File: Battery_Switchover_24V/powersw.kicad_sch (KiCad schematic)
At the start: 22 parts, among them U10 FDBL86066-F085, U2 LM74610QDGKRQ1, U5 LM74610QDGKRQ1

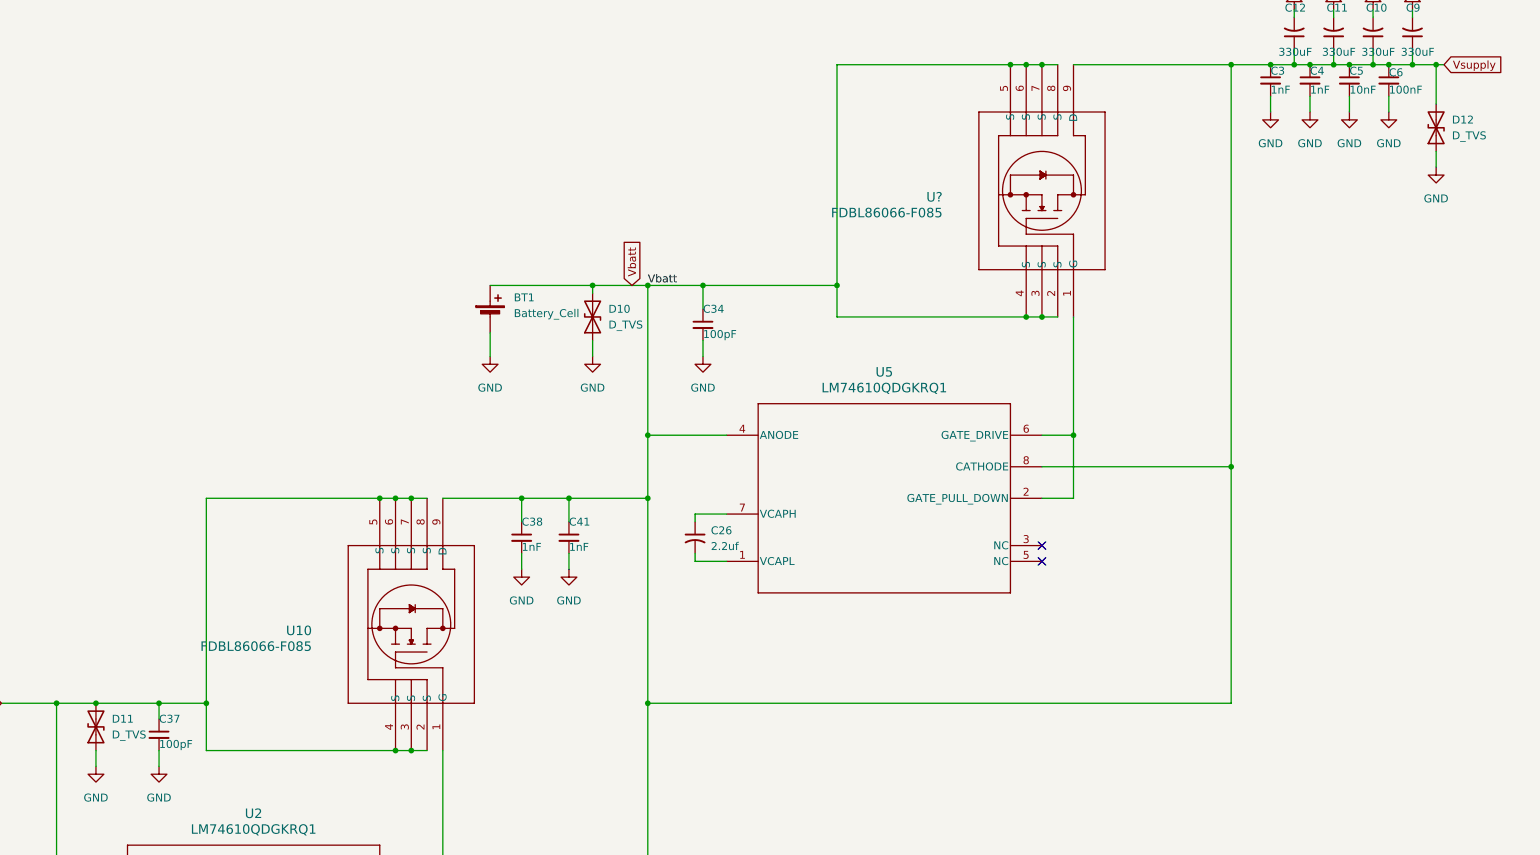
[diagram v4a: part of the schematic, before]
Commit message: Added some Model Numbers For TVS diodes
Added TVS diode model for ADC and
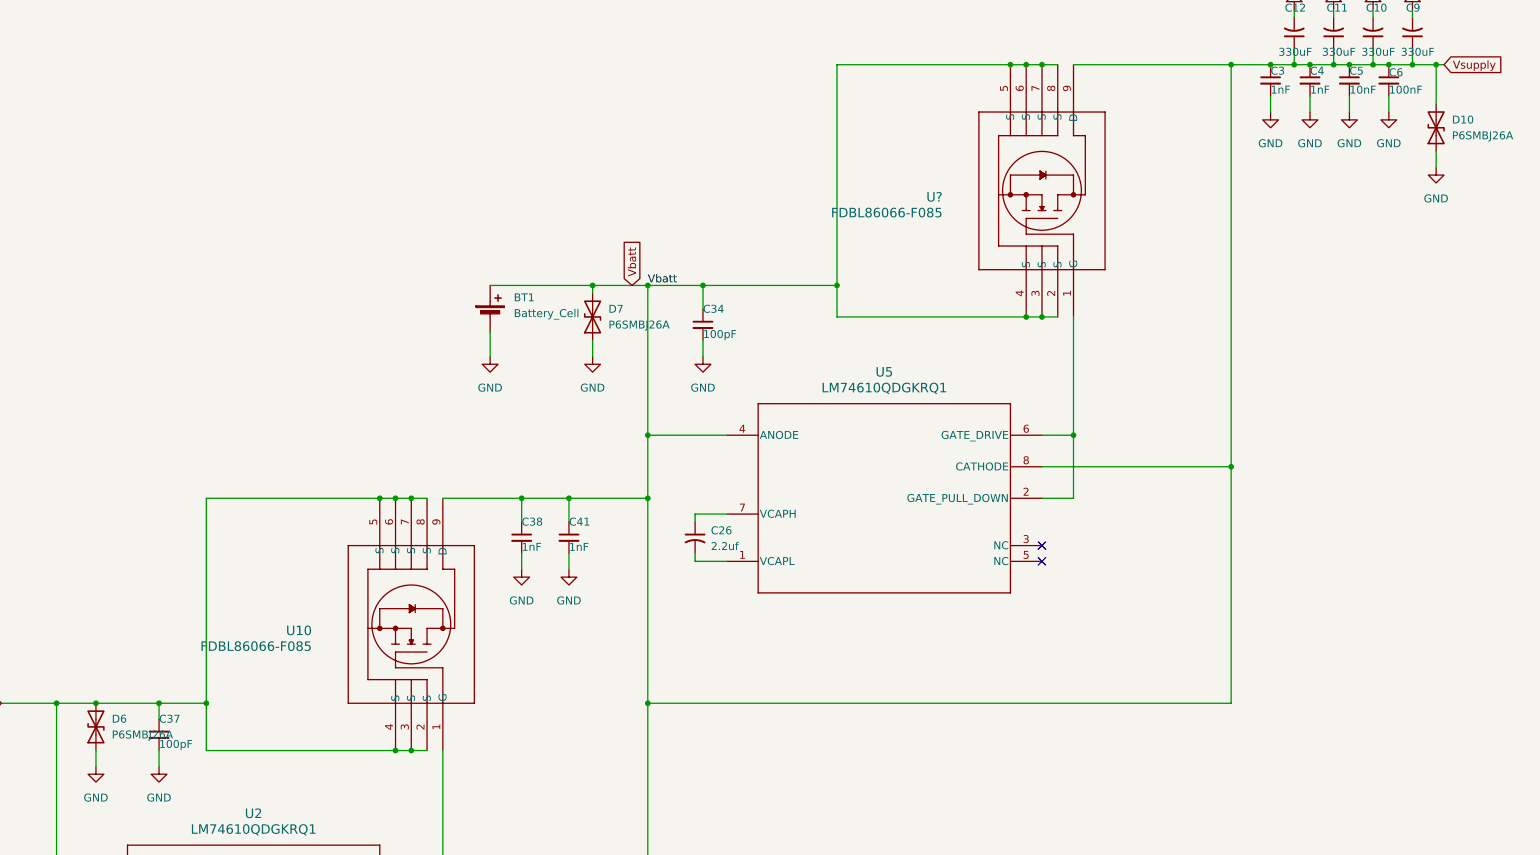
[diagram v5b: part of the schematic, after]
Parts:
- removed D11, D12: D_TVS, symbol Device:D_TVS
- added D6, D7: P6SMBJ26A, symbol Device:D_TVS
- D10: value D_TVS -> P6SMBJ26A
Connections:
- net GND: now also D6.1 (A1), D7.1 (A1)
- net Vbatt: now also D7.2 (A2)
- net Vin: now also D6.2 (A2)
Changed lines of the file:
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@@
 	)
 	(junction
+		(at 39.37 137.16)
+		(diameter 0)
+		(color 0 0 0 0)
+	)
+	(junction
 		(at 128.27 137.16)
 		(diameter 0)
@@
 	)
 	(junction
-		(at 39.37 137.16)
-		(diameter 0)
-		(color 0 0 0 0)
-	)
-	(junction
 		(at 119.38 69.85)
 		(diameter 0)
@@
 	(wire
 		(pts
+			(xy 39.37 137.16) (xy 49.53 137.16)
+		)
+		(stroke
+			(width 0)
+			(type default)
+		)
+	)
+	(wire
+		(pts
 			(xy 85.09 104.14) (xy 57.15 104.14)
 		)
@@
 	(wire
 		(pts
-			(xy 33.02 137.16) (xy 39.37 137.16)
-		)
-		(stroke
-			(width 0)
-			(type default)
-		)
-	)
-	(wire
-		(pts
 			(xy 49.53 144.78) (xy 49.53 147.32)
 		)
@@
 	(wire
 		(pts
-			(xy 39.37 137.16) (xy 49.53 137.16)
+			(xy 33.02 137.16) (xy 39.37 137.16)
 		)
 		(stroke
@@
 	)
 	(symbol
-		(lib_id "Device:D_TVS")
-		(at 119.38 74.93 90)
-		(unit 1)
-		(exclude_from_sim no)
-		(in_bom yes)
-		(on_board yes)
-		(dnp no)
-		(fields_autoplaced yes)
-		(property "Reference" "D10"
-			(at 121.92 73.6599 90)
-			(effects
-				(font
-					(size 1.27 1.27)
-				)
-				(justify right)
-			)
-		)
-		(property "Value" "D_TVS"
-			(at 121.92 76.1999 90)
-			(effects
-				(font
-					(size 1.27 1.27)
-				)
-				(justify right)
-			)
-		)
-		(property "Footprint" ""
-			(at 119.38 74.93 0)
-			(effects
-				(font
-					(size 1.27 1.27)
-				)
-				(hide yes)
-			)
-		)
-		(property "Datasheet" "~"
-			(at 119.38 74.93 0)
-			(effects
-				(font
-					(size 1.27 1.27)
-				)
-				(hide yes)
-			)
-		)
-		(property "Description" "Bidirectional transient-voltage-suppression diode"
-			(at 119.38 74.93 0)
-			(effects
-				(font
-					(size 1.27 1.27)
-				)
-				(hide yes)
-			)
-		)
-		(pin "2"
-		)
-		(pin "1"
-		)
-		(instances
-			(project "Battery_Switchover_24V"
-				(path "/045845e0-5d00-4da8-961e-99bdf190f683/40a8593a-1917-4d96-a386-ebab07cd1c69"
-					(reference "D10")
-					(unit 1)
-				)
-			)
-		)
-	)
-	(symbol
 		(lib_id "Device:C_Small")
 		(at 107.95 110.49 0)
@@
 	)
 	(symbol
-		(lib_id "Device:D_TVS")
-		(at 39.37 140.97 90)
-		(unit 1)
-		(exclude_from_sim no)
-		(in_bom yes)
-		(on_board yes)
-		(dnp no)
-		(fields_autoplaced yes)
-		(property "Reference" "D11"
-			(at 41.91 139.6999 90)
-			(effects
-				(font
-					(size 1.27 1.27)
-				)
-				(justify right)
-			)
-		)
-		(property "Value" "D_TVS"
-			(at 41.91 142.2399 90)
-			(effects
-				(font
-					(size 1.27 1.27)
-				)
-				(justify right)
-			)
-		)
-		(property "Footprint" ""
-			(at 39.37 140.97 0)
-			(effects
-				(font
-					(size 1.27 1.27)
-				)
-				(hide yes)
-			)
-		)
-		(property "Datasheet" "~"
-			(at 39.37 140.97 0)
-			(effects
-				(font
-					(size 1.27 1.27)
-				)
-				(hide yes)
-			)
-		)
-		(property "Description" "Bidirectional transient-voltage-suppression diode"
-			(at 39.37 140.97 0)
-			(effects
-				(font
-					(size 1.27 1.27)
-				)
-				(hide yes)
-			)
-		)
-		(pin "2"
-		)
-		(pin "1"
-		)
-		(instances
-			(project "Battery_Switchover_24V"
-				(path "/045845e0-5d00-4da8-961e-99bdf190f683/40a8593a-1917-4d96-a386-ebab07cd1c69"
-					(reference "D11")
-					(unit 1)
-				)
-			)
-		)
-	)
-	(symbol
-		(lib_id "Device:D_TVS")
-		(at 255.27 44.45 90)
-		(unit 1)
-		(exclude_from_sim no)
-		(in_bom yes)
-		(on_board yes)
-		(dnp no)
-		(fields_autoplaced yes)
-		(property "Reference" "D12"
-			(at 257.81 43.1799 90)
-			(effects
-				(font
-					(size 1.27 1.27)
-				)
-				(justify right)
-			)
-		)
-		(property "Value" "D_TVS"
-			(at 257.81 45.7199 90)
-			(effects
-				(font
-					(size 1.27 1.27)
-				)
-				(justify right)
-			)
-		)
-		(property "Footprint" ""
-			(at 255.27 44.45 0)
-			(effects
-				(font
-					(size 1.27 1.27)
-				)
-				(hide yes)
-			)
-		)
-		(property "Datasheet" "~"
-			(at 255.27 44.45 0)
-			(effects
-				(font
-					(size 1.27 1.27)
-				)
-				(hide yes)
-			)
-		)
-		(property "Description" "Bidirectional transient-voltage-suppression diode"
-			(at 255.27 44.45 0)
-			(effects
-				(font
-					(size 1.27 1.27)
-				)
-				(hide yes)
-			)
-		)
-		(pin "2"
-		)
-		(pin "1"
-		)
-		(instances
-			(project "Battery_Switchover_24V"
-				(path "/045845e0-5d00-4da8-961e-99bdf190f683/40a8593a-1917-4d96-a386-ebab07cd1c69"
-					(reference "D12")
-					(unit 1)
-				)
-			)
-		)
-	)
-	(symbol
 		(lib_id "power:GND")
 		(at 245.11 25.4 180)
@@
 	)
 	(symbol
+		(lib_id "Device:D_TVS")
+		(at 255.27 44.45 90)
+		(unit 1)
+		(exclude_from_sim no)
+		(in_bom yes)
+		(on_board yes)
+		(dnp no)
+		(fields_autoplaced yes)
+		(property "Reference" "D10"
+			(at 257.81 43.1799 90)
+			(effects
+				(font
+					(size 1.27 1.27)
+				)
+				(justify right)
+			)
+		)
+		(property "Value" "P6SMBJ26A"
+			(at 257.81 45.7199 90)
+			(effects
+				(font
+					(size 1.27 1.27)
+				)
+				(justify right)
+			)
+		)
+		(property "Footprint" ""
+			(at 255.27 44.45 0)
+			(effects
+				(font
+					(size 1.27 1.27)
+				)
+				(hide yes)
+			)
+		)
+		(property "Datasheet" "~"
+			(at 255.27 44.45 0)
+			(effects
+				(font
+					(size 1.27 1.27)
+				)
+				(hide yes)
+			)
+		)
+		(property "Description" "Bidirectional transient-voltage-suppression diode"
+			(at 255.27 44.45 0)
+			(effects
+				(font
+					(size 1.27 1.27)
+				)
+				(hide yes)
+			)
+		)
+		(pin "2"
+		)
+		(pin "1"
+		)
+		(instances
+			(project "Battery_Switchover_24V"
+				(path "/045845e0-5d00-4da8-961e-99bdf190f683/40a8593a-1917-4d96-a386-ebab07cd1c69"
+					(reference "D10")
+					(unit 1)
+				)
+			)
+		)
+	)
+	(symbol
 		(lib_id "Device:C_Small")
 		(at 49.53 142.24 0)
@@
 	)
 	(symbol
+		(lib_id "Device:D_TVS")
+		(at 119.38 74.93 90)
+		(unit 1)
+		(exclude_from_sim no)
+		(in_bom yes)
+		(on_board yes)
+		(dnp no)
+		(fields_autoplaced yes)
+		(property "Reference" "D7"
+			(at 121.92 73.6599 90)
+			(effects
+				(font
+					(size 1.27 1.27)
+				)
+				(justify right)
+			)
+		)
+		(property "Value" "P6SMBJ26A"
+			(at 121.92 76.1999 90)
+			(effects
+				(font
+					(size 1.27 1.27)
+				)
+				(justify right)
+			)
+		)
+		(property "Footprint" ""
+			(at 119.38 74.93 0)
+			(effects
+				(font
+					(size 1.27 1.27)
+				)
+				(hide yes)
+			)
+		)
+		(property "Datasheet" "~"
+			(at 119.38 74.93 0)
+			(effects
+				(font
+					(size 1.27 1.27)
+				)
+				(hide yes)
+			)
+		)
+		(property "Description" "Bidirectional transient-voltage-suppression diode"
+			(at 119.38 74.93 0)
+			(effects
+				(font
+					(size 1.27 1.27)
+				)
+				(hide yes)
+			)
+		)
+		(pin "2"
+		)
+		(pin "1"
+		)
+		(instances
+			(project "Battery_Switchover_24V"
+				(path "/045845e0-5d00-4da8-961e-99bdf190f683/40a8593a-1917-4d96-a386-ebab07cd1c69"
+					(reference "D7")
+					(unit 1)
+				)
+			)
+		)
+	)
+	(symbol
 		(lib_id "power:GND")
 		(at 115.57 115.57 0)
@@
 					(unit 1)
 				)
+			)
+		)
+	)
+	(symbol
+		(lib_id "Device:D_TVS")
+		(at 39.37 140.97 90)
+		(unit 1)
+		(exclude_from_sim no)
+		(in_bom yes)
+		(on_board yes)
+		(dnp no)
+		(fields_autoplaced yes)
+		(property "Reference" "D6"
+			(at 41.91 139.6999 90)
+			(effects
+				(font
+					(size 1.27 1.27)
+				)
+				(justify right)
+			)
+		)
+		(property "Value" "P6SMBJ26A"
+			(at 41.91 142.2399 90)
+			(effects
+				(font
+					(size 1.27 1.27)
+				)
+				(justify right)
+			)
+		)
+		(property "Footprint" ""
+			(at 39.37 140.97 0)
+			(effects
+				(font
+					(size 1.27 1.27)
+				)
+				(hide yes)
+			)
+		)
+		(property "Datasheet" "~"
+			(at 39.37 140.97 0)
+			(effects
+				(font
+					(size 1.27 1.27)
+				)
+				(hide yes)
+			)
+		)
+		(property "Description" "Bidirectional transient-voltage-suppression diode"
+			(at 39.37 140.97 0)
+			(effects
+				(font
+					(size 1.27 1.27)
+				)
+				(hide yes)
+			)
+		)
+		(pin "2"
+		)
+		(pin "1"
+		)
+		(instances
+			(project "Battery_Switchover_24V"
+				(path "/045845e0-5d00-4da8-961e-99bdf190f683/40a8593a-1917-4d96-a386-ebab07cd1c69"
+					(reference "D6")
+					(unit 1)
+				)

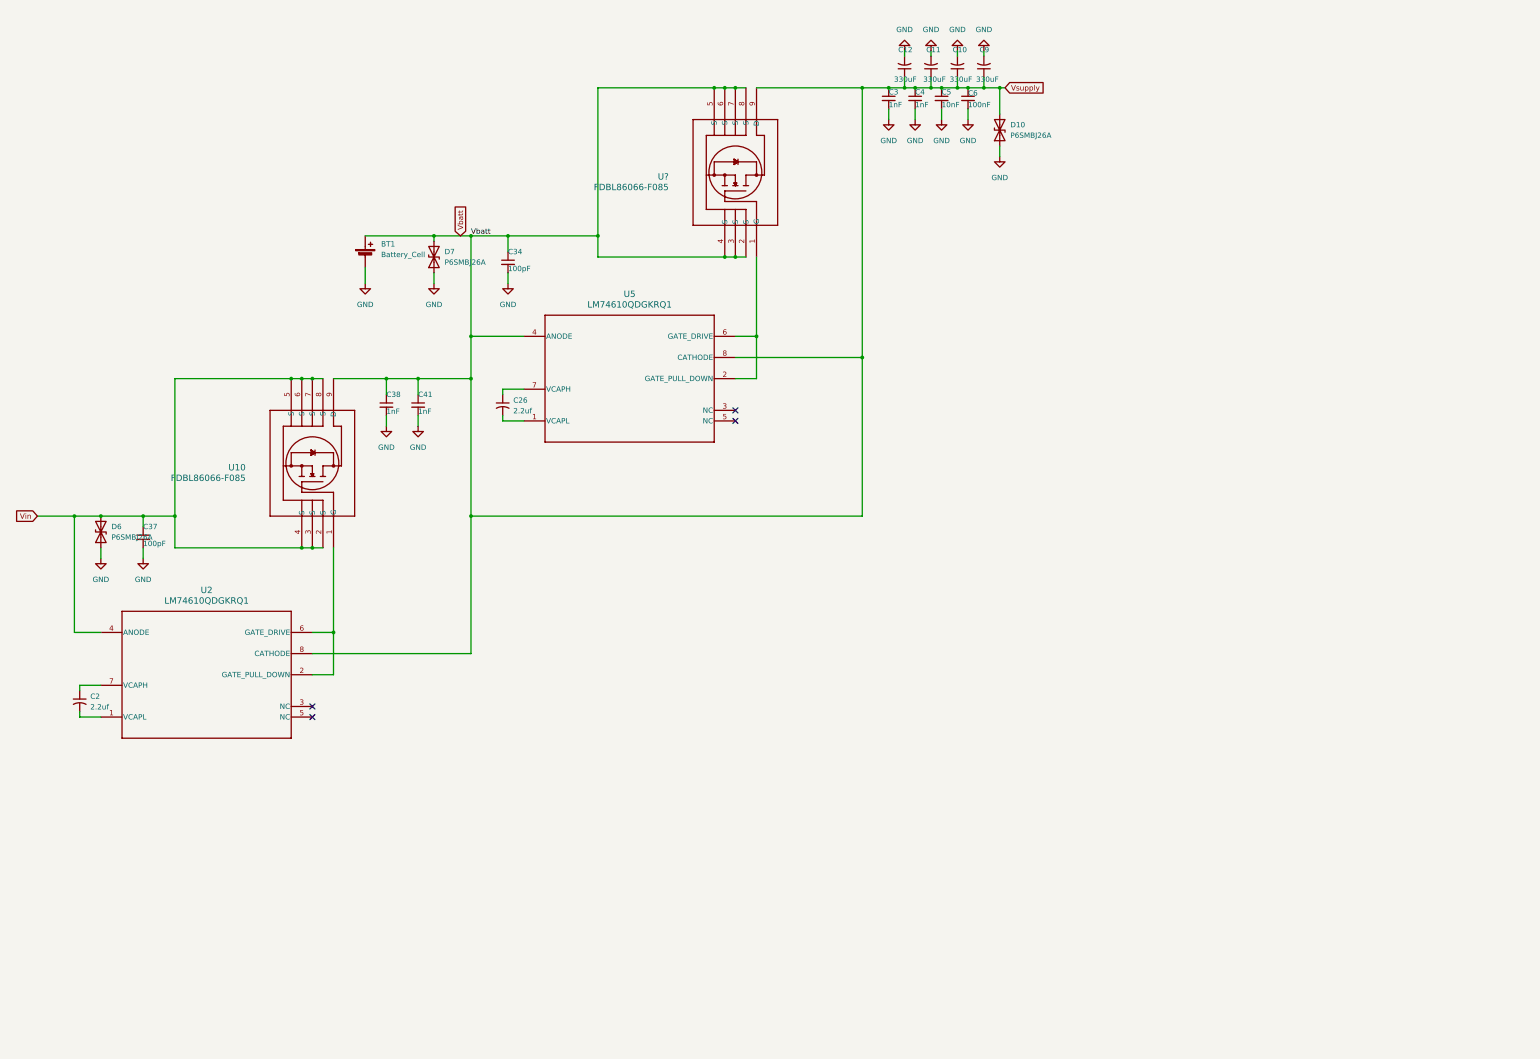
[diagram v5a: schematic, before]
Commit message: Added Some Footprints
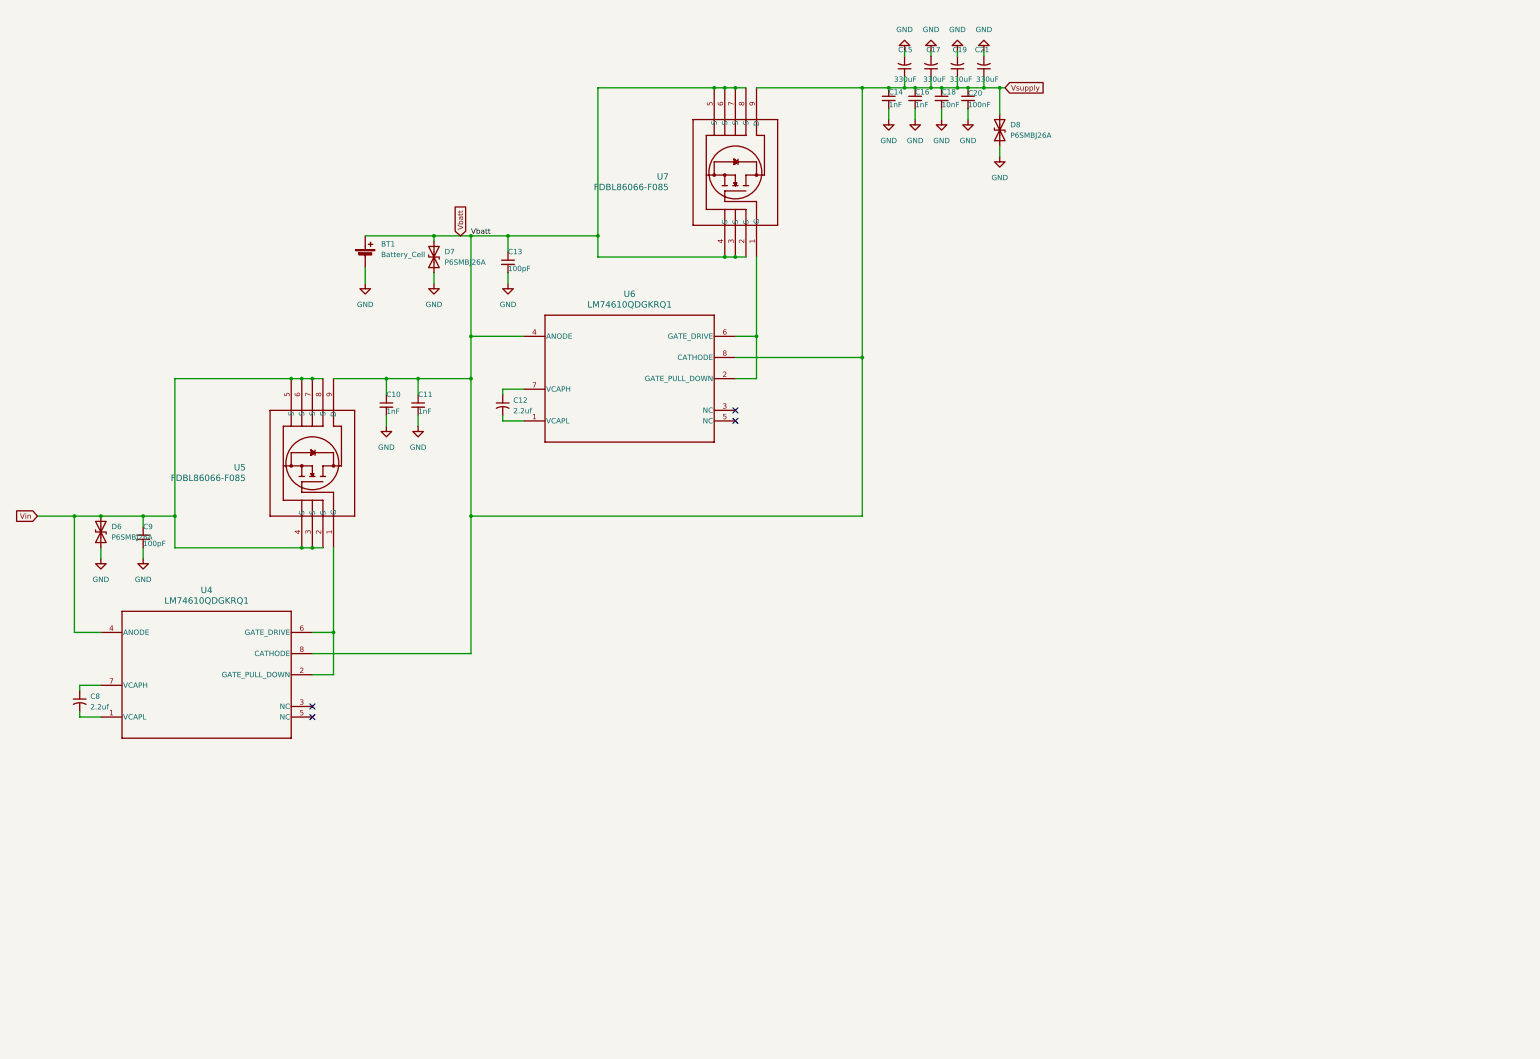
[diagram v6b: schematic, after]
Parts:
- C10: renamed from C38; footprint (none) -> Capacitor_SMD:C_0603_1608Metric
- C11: renamed from C41; footprint (none) -> Capacitor_SMD:C_0603_1608Metric
- C13: renamed from C34; footprint (none) -> Capacitor_SMD:C_0603_1608Metric
- C14: renamed from C3; footprint (none) -> Capacitor_SMD:C_0402_1005Metric
- C15: renamed from C12; footprint (none) -> Capacitor_THT:CP_Radial_Tantal_D10.5mm_P5.00mm
- C16: renamed from C4; footprint (none) -> Capacitor_SMD:C_0402_1005Metric
- C17: renamed from C11; footprint (none) -> Capacitor_THT:CP_Radial_Tantal_D10.5mm_P5.00mm
- C18: renamed from C5; footprint (none) -> Capacitor_SMD:C_0603_1608Metric
- C19: renamed from C10; footprint (none) -> Capacitor_THT:CP_Radial_Tantal_D10.5mm_P5.00mm
- C20: renamed from C6; footprint (none) -> Capacitor_SMD:C_0603_1608Metric
- C21: renamed from C9; footprint (none) -> Capacitor_THT:CP_Radial_Tantal_D10.5mm_P5.00mm
- C9: renamed from C37; footprint (none) -> Capacitor_SMD:C_0603_1608Metric
- D6, D7: footprint (none) -> footprints:P26_DO-214AA_SMB
- D8: renamed from D10; footprint (none) -> footprints:P26_DO-214AA_SMB
- U4: renamed from U2; footprint DGK0008A_N -> footprints:DGK0008A_N
- U6: renamed from U5; footprint DGK0008A_N -> footprints:DGK0008A_N
- gave numbers to parts that had none: 1
- renumbered C26 to C12, C2 to C8, U10 to U5
